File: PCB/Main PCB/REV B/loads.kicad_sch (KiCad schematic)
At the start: 13 parts, among them J10 Ignitor, J11 Auger, J12 FAN, K1 CPC1966Y, U8 AQH3223A, U9 AQH3223A

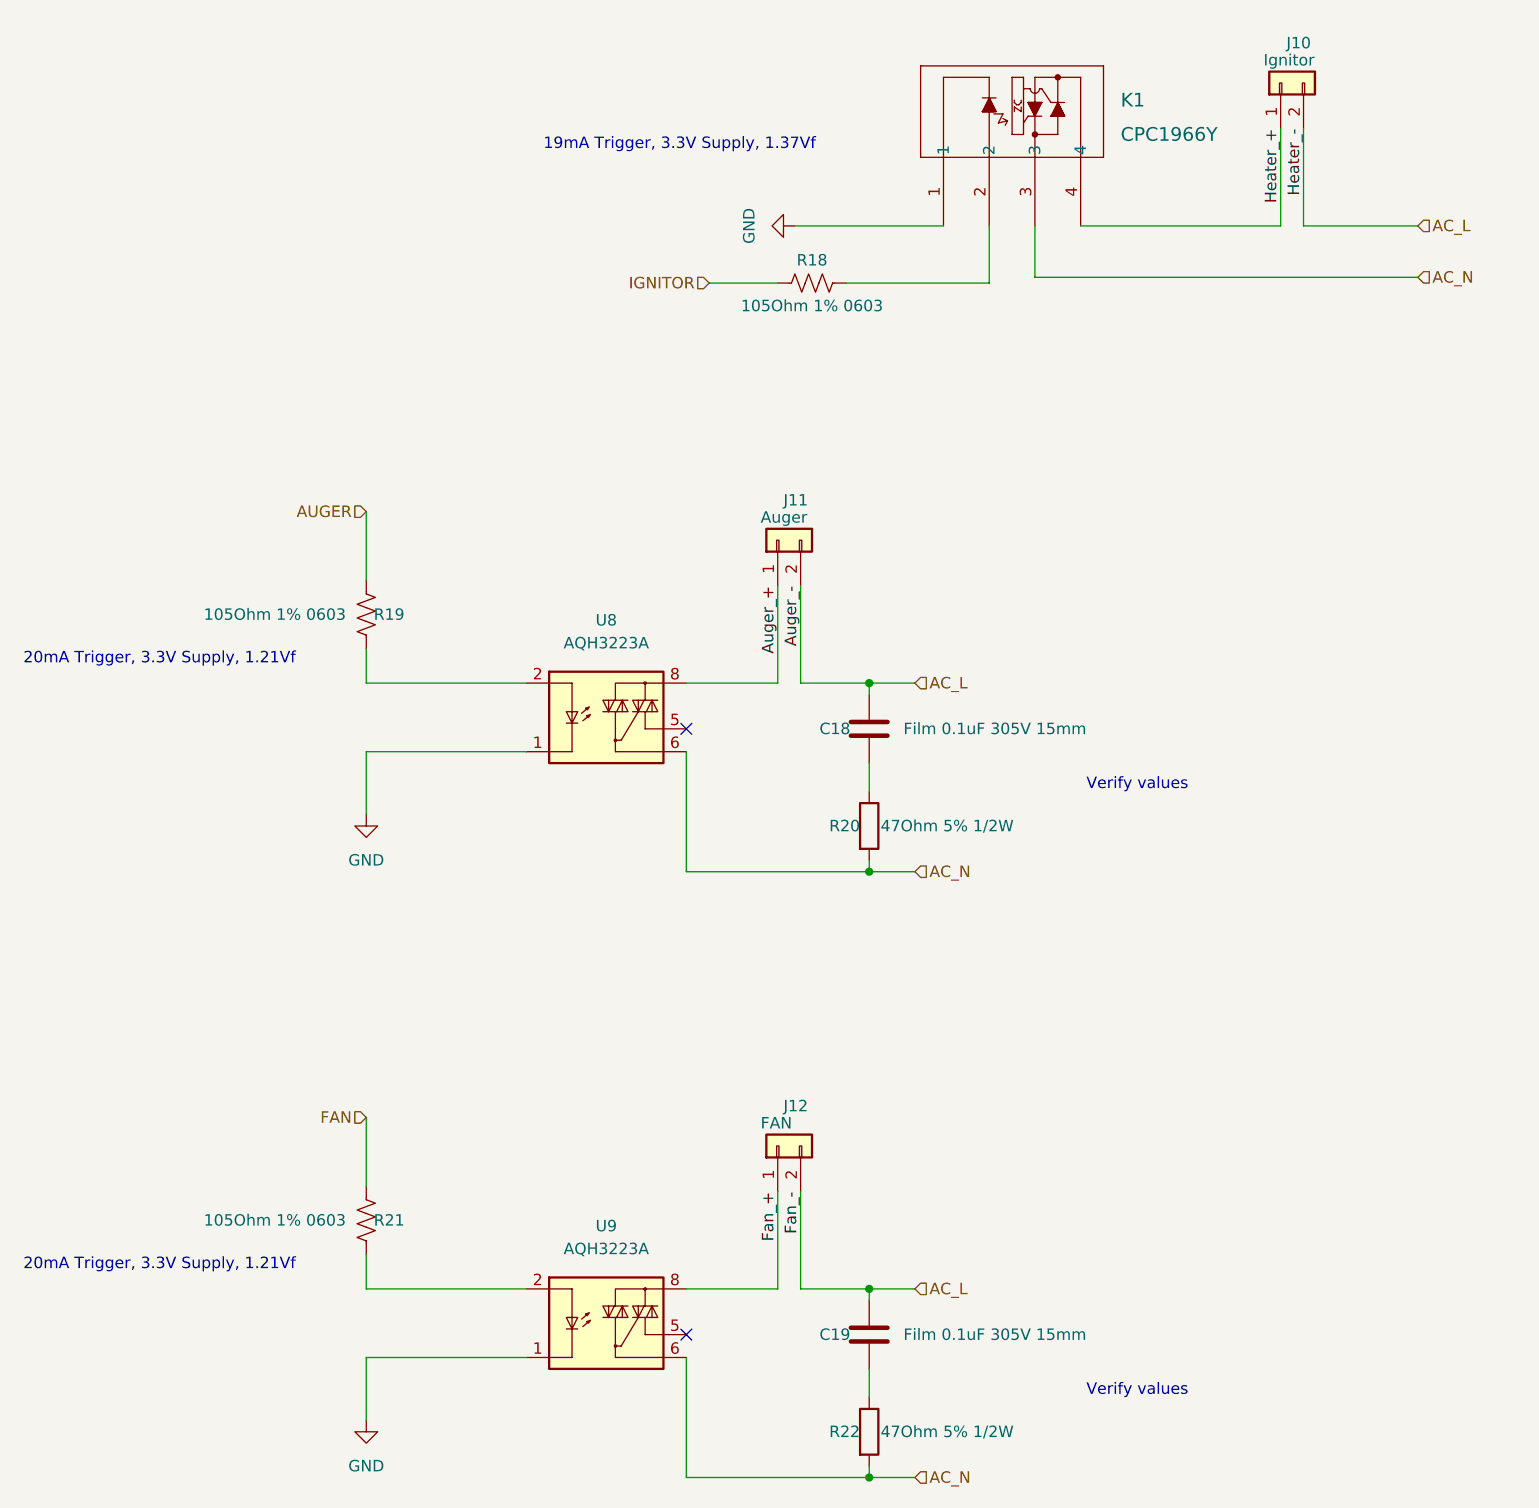
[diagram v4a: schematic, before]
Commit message: Changed rotary encoder to incremental, nearly done design on rotary encoder
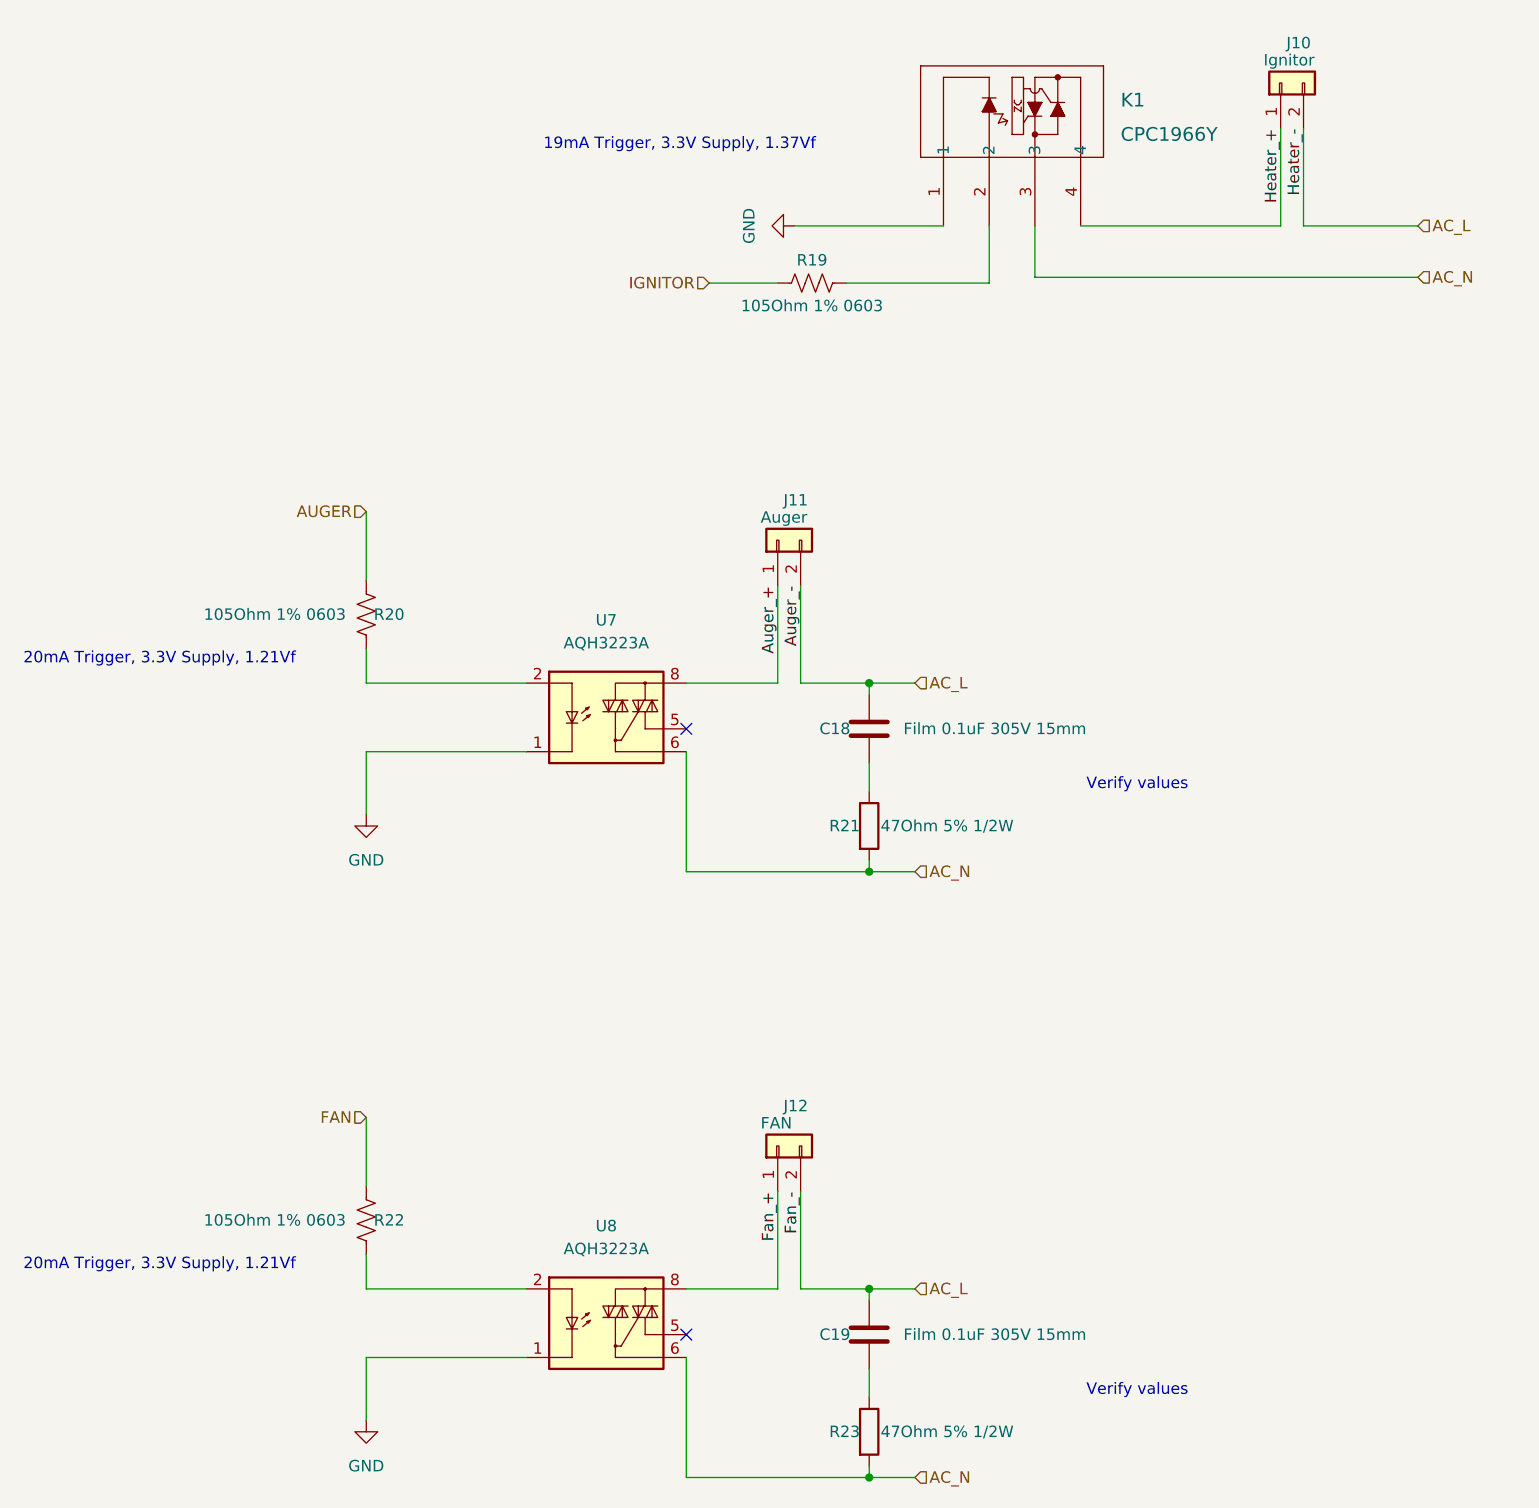
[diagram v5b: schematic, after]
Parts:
- renumbered R18 to R19, R19 to R20, R20 to R21, R21 to R22, R22 to R23, U8 to U7, U9 to U8
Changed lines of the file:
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@@
   (symbol (lib_id "Relay_SolidState:AQH3223A") (at 102.87 172.085 0) (unit 1)
     (in_bom yes) (on_board yes) (fields_autoplaced)
-    (property "Reference" "U9" (id 0) (at 101.6 162.56 0))
+    (property "Reference" "U8" (id 0) (at 101.6 162.56 0))
     (property "Value" "AQH3223A" (id 1) (at 101.6 165.1 0))
     (property "Footprint" "Package_SO:SSO-7-8_6.4x9.78mm_P2.54mm" (id 2) (at 95.25 177.165 0)
@@
   (symbol (lib_id "Relay_SolidState:AQH3223A") (at 102.87 104.775 0) (unit 1)
     (in_bom yes) (on_board yes) (fields_autoplaced)
-    (property "Reference" "U8" (id 0) (at 101.6 95.25 0))
+    (property "Reference" "U7" (id 0) (at 101.6 95.25 0))
     (property "Value" "AQH3223A" (id 1) (at 101.6 97.79 0))
     (property "Footprint" "Package_SO:SSO-7-8_6.4x9.78mm_P2.54mm" (id 2) (at 95.25 109.855 0)
@@
   (symbol (lib_id "Device:R") (at 130.81 118.11 0) (unit 1)
     (in_bom yes) (on_board yes)
-    (property "Reference" "R20" (id 0) (at 126.365 118.11 0)
+    (property "Reference" "R21" (id 0) (at 126.365 118.11 0)
       (effects (font (size 1.27 1.27)) (justify left))
     )
@@
   (symbol (lib_id "power:GND") (at 74.93 116.84 0) (mirror y) (unit 1)
     (in_bom yes) (on_board yes)
-    (property "Reference" "#PWR061" (id 0) (at 74.93 123.19 0)
+    (property "Reference" "#PWR063" (id 0) (at 74.93 123.19 0)
       (effects (font (size 1.27 1.27)) hide)
     )
@@
   (symbol (lib_id "Device:R_US") (at 74.93 161.925 0) (unit 1)
     (in_bom yes) (on_board yes)
-    (property "Reference" "R21" (id 0) (at 77.47 161.925 0))
+    (property "Reference" "R22" (id 0) (at 77.47 161.925 0))
     (property "Value" "105Ohm 1% 0603" (id 1) (at 64.77 161.925 0))
     (property "Footprint" "Resistor_SMD:R_0603_1608Metric" (id 2) (at 75.946 162.179 90)
@@
   (symbol (lib_id "power:GND") (at 74.93 184.15 0) (mirror y) (unit 1)
     (in_bom yes) (on_board yes)
-    (property "Reference" "#PWR062" (id 0) (at 74.93 190.5 0)
+    (property "Reference" "#PWR064" (id 0) (at 74.93 190.5 0)
       (effects (font (size 1.27 1.27)) hide)
     )
@@
   (symbol (lib_id "Device:R") (at 130.81 185.42 0) (unit 1)
     (in_bom yes) (on_board yes)
-    (property "Reference" "R22" (id 0) (at 126.365 185.42 0)
+    (property "Reference" "R23" (id 0) (at 126.365 185.42 0)
       (effects (font (size 1.27 1.27)) (justify left))
     )
@@
   (symbol (lib_id "Device:R_US") (at 74.93 94.615 0) (unit 1)
     (in_bom yes) (on_board yes)
-    (property "Reference" "R19" (id 0) (at 77.47 94.615 0))
+    (property "Reference" "R20" (id 0) (at 77.47 94.615 0))
     (property "Value" "105Ohm 1% 0603" (id 1) (at 64.77 94.615 0))
     (property "Footprint" "Resistor_SMD:R_0603_1608Metric" (id 2) (at 75.946 94.869 90)
@@
   (symbol (lib_id "Device:R_US") (at 124.46 57.785 90) (unit 1)
     (in_bom yes) (on_board yes)
-    (property "Reference" "R18" (id 0) (at 124.46 55.245 90))
+    (property "Reference" "R19" (id 0) (at 124.46 55.245 90))
     (property "Value" "105Ohm 1% 0603" (id 1) (at 124.46 60.325 90))
     (property "Footprint" "Resistor_SMD:R_0603_1608Metric" (id 2) (at 124.714 56.769 90)
@@
   (symbol (lib_id "power:GND") (at 122.555 51.435 270) (mirror x) (unit 1)
     (in_bom yes) (on_board yes)
-    (property "Reference" "#PWR060" (id 0) (at 116.205 51.435 0)
-      (effects (font (size 1.27 1.27)) hide)
-    )
+    (property "Reference" "#PWR062" (id 0) (at 116.205 51.435 0)
+      (effects (font (size 1.27 1.27)) hide)
+    )

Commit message: SD card complete. All gpio full
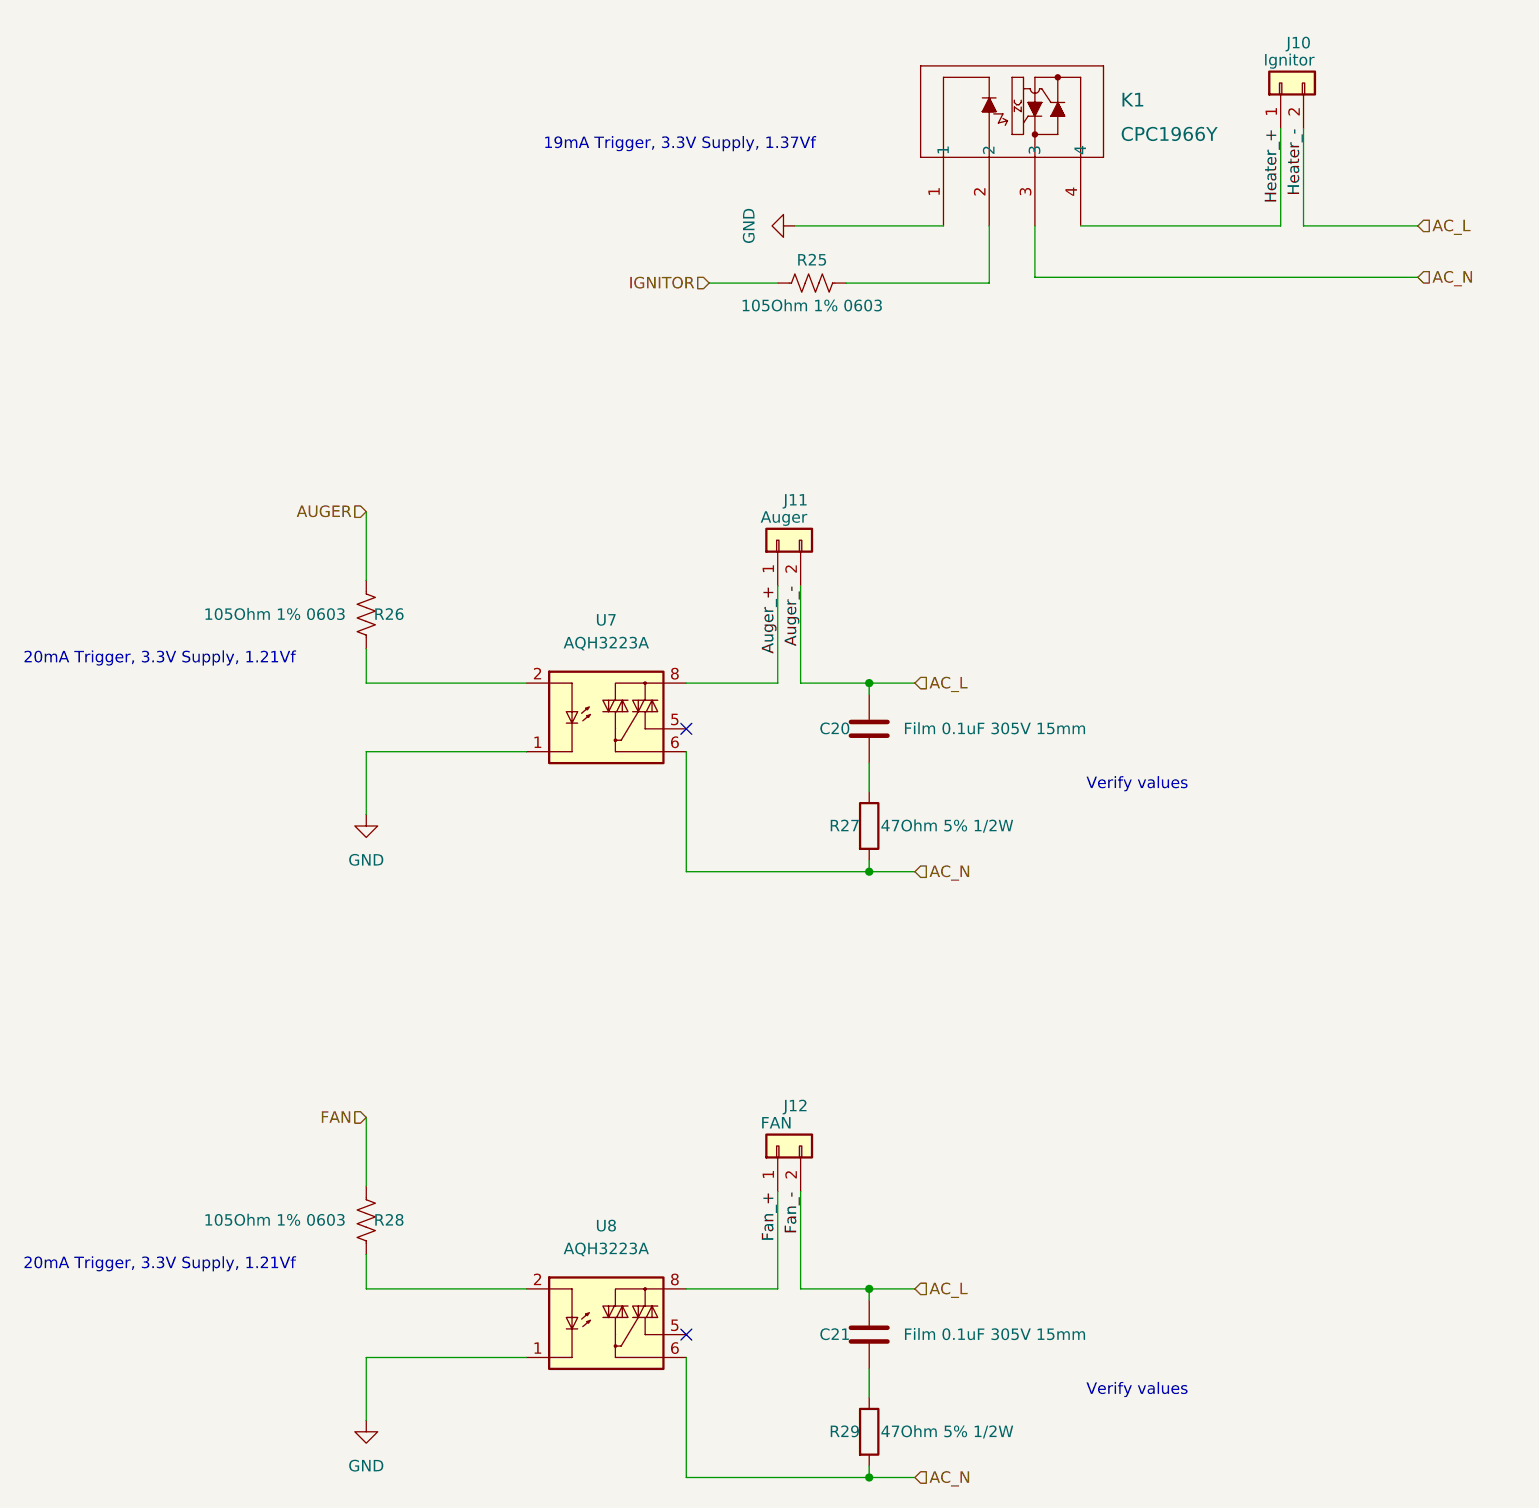
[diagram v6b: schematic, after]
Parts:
- renumbered C18 to C20, C19 to C21, R19 to R25, R20 to R26, R21 to R27, R22 to R28, R23 to R29
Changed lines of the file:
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@@
   (symbol (lib_id "Device:C") (at 130.81 107.315 0) (unit 1)
     (in_bom yes) (on_board yes)
-    (property "Reference" "C18" (id 0) (at 127 107.315 0))
+    (property "Reference" "C20" (id 0) (at 127 107.315 0))
     (property "Value" "Film 0.1uF 305V 15mm" (id 1) (at 144.78 107.315 0))
     (property "Footprint" "Capacitor_THT:C_Rect_L18.0mm_W6.0mm_P15.00mm_FKS3_FKP3" (id 2) (at 131.7752 111.125 0)
@@
   (symbol (lib_id "Device:C") (at 130.81 174.625 0) (unit 1)
     (in_bom yes) (on_board yes)
-    (property "Reference" "C19" (id 0) (at 127 174.625 0))
+    (property "Reference" "C21" (id 0) (at 127 174.625 0))
     (property "Value" "Film 0.1uF 305V 15mm" (id 1) (at 144.78 174.625 0))
     (property "Footprint" "Capacitor_THT:C_Rect_L18.0mm_W6.0mm_P15.00mm_FKS3_FKP3" (id 2) (at 131.7752 178.435 0)
@@
   (symbol (lib_id "Device:R") (at 130.81 118.11 0) (unit 1)
     (in_bom yes) (on_board yes)
-    (property "Reference" "R21" (id 0) (at 126.365 118.11 0)
+    (property "Reference" "R27" (id 0) (at 126.365 118.11 0)
       (effects (font (size 1.27 1.27)) (justify left))
     )
@@
   (symbol (lib_id "power:GND") (at 74.93 116.84 0) (mirror y) (unit 1)
     (in_bom yes) (on_board yes)
-    (property "Reference" "#PWR063" (id 0) (at 74.93 123.19 0)
+    (property "Reference" "#PWR072" (id 0) (at 74.93 123.19 0)
       (effects (font (size 1.27 1.27)) hide)
     )
@@
   (symbol (lib_id "Device:R_US") (at 74.93 161.925 0) (unit 1)
     (in_bom yes) (on_board yes)
-    (property "Reference" "R22" (id 0) (at 77.47 161.925 0))
+    (property "Reference" "R28" (id 0) (at 77.47 161.925 0))
     (property "Value" "105Ohm 1% 0603" (id 1) (at 64.77 161.925 0))
     (property "Footprint" "Resistor_SMD:R_0603_1608Metric" (id 2) (at 75.946 162.179 90)
@@
   (symbol (lib_id "power:GND") (at 74.93 184.15 0) (mirror y) (unit 1)
     (in_bom yes) (on_board yes)
-    (property "Reference" "#PWR064" (id 0) (at 74.93 190.5 0)
+    (property "Reference" "#PWR073" (id 0) (at 74.93 190.5 0)
       (effects (font (size 1.27 1.27)) hide)
     )
@@
   (symbol (lib_id "Device:R") (at 130.81 185.42 0) (unit 1)
     (in_bom yes) (on_board yes)
-    (property "Reference" "R23" (id 0) (at 126.365 185.42 0)
+    (property "Reference" "R29" (id 0) (at 126.365 185.42 0)
       (effects (font (size 1.27 1.27)) (justify left))
     )
@@
   (symbol (lib_id "Device:R_US") (at 74.93 94.615 0) (unit 1)
     (in_bom yes) (on_board yes)
-    (property "Reference" "R20" (id 0) (at 77.47 94.615 0))
+    (property "Reference" "R26" (id 0) (at 77.47 94.615 0))
     (property "Value" "105Ohm 1% 0603" (id 1) (at 64.77 94.615 0))
     (property "Footprint" "Resistor_SMD:R_0603_1608Metric" (id 2) (at 75.946 94.869 90)
@@
   (symbol (lib_id "Device:R_US") (at 124.46 57.785 90) (unit 1)
     (in_bom yes) (on_board yes)
-    (property "Reference" "R19" (id 0) (at 124.46 55.245 90))
+    (property "Reference" "R25" (id 0) (at 124.46 55.245 90))
     (property "Value" "105Ohm 1% 0603" (id 1) (at 124.46 60.325 90))
     (property "Footprint" "Resistor_SMD:R_0603_1608Metric" (id 2) (at 124.714 56.769 90)
@@
   (symbol (lib_id "power:GND") (at 122.555 51.435 270) (mirror x) (unit 1)
     (in_bom yes) (on_board yes)
-    (property "Reference" "#PWR062" (id 0) (at 116.205 51.435 0)
-      (effects (font (size 1.27 1.27)) hide)
-    )
+    (property "Reference" "#PWR071" (id 0) (at 116.205 51.435 0)
+      (effects (font (size 1.27 1.27)) hide)
+    )

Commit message: Begin layout Rev B PCB
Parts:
- renumbered C20 to C21, C21 to C22
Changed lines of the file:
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@@
   (symbol (lib_id "Device:C") (at 130.81 107.315 0) (unit 1)
     (in_bom yes) (on_board yes)
-    (property "Reference" "C20" (id 0) (at 127 107.315 0))
+    (property "Reference" "C21" (id 0) (at 127 107.315 0))
     (property "Value" "Film 0.1uF 305V 15mm" (id 1) (at 144.78 107.315 0))
     (property "Footprint" "Capacitor_THT:C_Rect_L18.0mm_W6.0mm_P15.00mm_FKS3_FKP3" (id 2) (at 131.7752 111.125 0)
@@
   (symbol (lib_id "Device:C") (at 130.81 174.625 0) (unit 1)
     (in_bom yes) (on_board yes)
-    (property "Reference" "C21" (id 0) (at 127 174.625 0))
+    (property "Reference" "C22" (id 0) (at 127 174.625 0))
     (property "Value" "Film 0.1uF 305V 15mm" (id 1) (at 144.78 174.625 0))
     (property "Footprint" "Capacitor_THT:C_Rect_L18.0mm_W6.0mm_P15.00mm_FKS3_FKP3" (id 2) (at 131.7752 178.435 0)
